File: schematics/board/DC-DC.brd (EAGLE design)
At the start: 91 x 60 mm, 130 parts

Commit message: Плата DC-DC
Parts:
- added 3,3µH: 3,3µ, CanCubeSat:B82472G6
- added 3,3µH1: 3,3µH, CanCubeSat:B82472G6
- added C40, C41, C49, C50, C56: 0,1µ, rcl:C0603
- added C44, C52: 680p, rcl:C0603
- added C45, C53: 4.7µ, rcl:C1206
- added C46: 3,3n, rcl:C0603
- added C47, C54: 150µ, CanCubeSat:ECAP150
- added C48, C55: 220µ, CanCubeSat:ECAP220
- added C57: 10µ, rcl:C1206
- added INVERT: INVERTER, CanCubeSat:SOT23-5
- added LED_G1, LED_G2, LED_R1, LED_R2: (no value), led:CHIPLED_0603
- added OPA: OPA333, CanCubeSat:SOT23-5
- added R100, R32, R33, R57: 2k, resistor:R0603
- added R28, R30, R37, R39, R67, R68, R69: 150k, resistor:R0603
- added R34, R35: 51k, resistor:R0603
- added R36, R38, R66: 10k, resistor:R0603
- added R40: 910k, resistor:R0603
- added R41: 330k, resistor:R0603
- added R65: 1M, resistor:R0603
- added R70: 24k3, resistor:R0603
- added R72: 232k, resistor:R0603
- added U$23, U$59: LTC31191, CanCubeSat:LTC3119+VIA
- added U$25: 32961, CanCubeSat:3296W
- U$2: device CanCubeSat:B82477G4 -> CanCubeSat:L_12X12
- U$3: device CanCubeSat:MP2225 -> CanCubeSat:TSOT23-8
- U$4: device CanCubeSat:SPM5020 -> CanCubeSat:L_SPM5020
- U$6, U$7: device CanCubeSat:SPM4020 -> CanCubeSat:L_SPM4020
- moved U$6 0.46 mm to (66.3, 23.6)
- moved U$4 0.28 mm to (22.2, 25.8)
- moved U$2 0.21 mm to (38.2, 23.9)
- moved U$3 0.07 mm to (8.00, 26.1)
- moved U$7 0.07 mm to (74.2, 23.6)
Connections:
- new net 1.65: R34.2, R35.1, R36.2
- new net 3.3: INVERT.P$5, OPA.P$5, R35.2
- new net 90: R65.1, R66.2, R67.2, U$59.15
- new net A: INVERT.P$2, OPA.P$1, R32.1, R37.2, R39.2, U$59.18
- new net INA_BMS+: C47.P$1, C55.P$1, R72.2, U$23.19, U$23.22, U$23.23, U$59.6, U$59.7
- new net INA_BUS+: C48.P$1, C54.P$1, R40.1, R65.2, U$23.6, U$23.7, U$25.P$3, U$59.19, U$59.22, U$59.23
- new net N$129: C41.2, U$59.3
- new net N$131: 3,3µH.2, C40.1, U$59.21, U$59.24
- new net N$132: 3,3µH.1, C41.1, U$59.5, U$59.8
- new net N$135: R69.1, U$59.13
- new net N$136: C44.1, R69.2
- new net N$139: C46.1, R66.1
- new net N$142: R68.2, U$59.17
- new net N$144: C40.2, U$59.26
- new net N$215: C53.1, C56.1, C57.1, LED_G2.A, U$23.11, U$23.15, U$23.16
- new net N$234: C45.1, LED_G1.A, U$59.11, U$59.16
- new net N$302: OPA.P$4, R36.1, R37.1
- new net N$77: 3,3µH1.2, C49.1, U$23.21, U$23.24
- new net N$78: 3,3µH1.1, C50.1, U$23.5, U$23.8
- new net N$79: R28.2, U$23.17
- new net N$80: C49.2, U$23.26
- new net N$81: R30.1, U$23.13
- new net N$82: C52.1, R30.2
- new net N$84: C50.2, U$23.3
- new net N$85: LED_R1.A, R32.2
- new net N$86: U$23.12, U$25.P$2
- new net N$87: LED_R2.A, R57.2
- new net N$89: R70.1, R72.1, U$59.12
- new net N$90: OPA.P$3, R38.1, R39.1
- new net N$91: LED_G1.C, R100.2
- new net N$92: LED_G2.C, R33.2
- new net PGOOD1: LED_R1.C, U$59.10
- new net PGOOD2: LED_R2.C, U$23.10
- new net RUN: R38.2, R40.2, R41.1
- new net Y: INVERT.P$4, R57.1, U$23.18
- net GND: now also C44.2, C45.2, C46.2, C47.P$2, C48.P$2, C52.2, C53.2, C54.P$2, C55.P$2, C56.2, C57.2, INVERT.P$3, OPA.P$2, R100.1, R28.1, R33.1, R34.1, R41.2, R67.1, R68.1, R70.2, U$23.14, U$23.20, U$23.25, U$23.28, U$23.29, U$23.4, U$23.9, U$23.P$1, U$23.P$10, U$23.P$2, U$23.P$3, U$23.P$4, U$23.P$5, U$23.P$6, U$23.P$7, U$23.P$8, U$23.P$9, U$25.P$1, U$59.14, U$59.20, U$59.25, U$59.28, U$59.29, U$59.4, U$59.9, U$59.P$1, U$59.P$10, U$59.P$2, U$59.P$3, U$59.P$4, U$59.P$5, U$59.P$6, U$59.P$7, U$59.P$8, U$59.P$9
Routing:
- net GND: track 57.0 -> 167.3 mm, vias 54 -> 63
- net INA_BUS+: track 0.00 -> 95.3 mm, vias 0 -> 9
- net INA_BMS+: track 0.00 -> 78.7 mm, vias 0 -> 7
- net A: track 0.00 -> 65.3 mm, vias 0 -> 4
- net Y: track 0.00 -> 48.8 mm, vias 0 -> 4
- net PGOOD2: track 0.00 -> 35.8 mm, vias 0 -> 2
- net PGOOD1: track 0.00 -> 32.1 mm, vias 0 -> 2
- net 3.3: track 0.00 -> 20.9 mm, vias 0 -> 1
- net N$234: track 0.00 -> 19.3 mm, vias 0 -> 2
- net 90: track 0.00 -> 18.2 mm, vias 0 -> 3
- net N$215: track 0.00 -> 18.1 mm, vias 0 -> 2
- net N$86: track 0.00 -> 14.3 mm
- net N$89: track 0.00 -> 11.7 mm
- net N$142: track 0.00 -> 9.93 mm
- net N$79: track 0.00 -> 9.65 mm
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- added copper zone on layer 1, net INA_BMS+
- added copper zone on layer 16, net INA_BMS+
- added copper zone on layer 1, net INA_BUS+
- added copper zone on layer 16, net INA_BUS+
- added copper zone on layer 1, net N$131
- added copper zone on layer 1, net N$132
- added copper zone on layer 1, net N$215
- added copper zone on layer 1, net N$234
- added copper zone on layer 1, net N$77
- added copper zone on layer 1, net N$78
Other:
- board size 91 x 60 mm -> 91 x 91 mm
- board text added: "BMS+"
- board text added: "BUS+"

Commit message: платы DC-DC и AB
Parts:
- removed D1: MBR0520LT, diode:SOD123
- added D2: (no value), diode:SMC
- moved C2 7.20 mm to (35.9, 44.6)
- moved C36 7.20 mm to (45.6, 45.2)
- moved C4 7.20 mm to (41.0, 51.2)
- moved R10 7.20 mm to (48.0, 45.2)
- moved R3 7.20 mm to (43.3, 51.0)
- moved R4 7.20 mm to (46.0, 41.2)
- moved R6 7.20 mm to (35.9, 48.6)
- moved R7 7.20 mm to (33.5, 48.6)
- moved U$1 7.20 mm to (41.0, 44.2)
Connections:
- net GND: now also D2.A; no longer D1.A
- net N$6: now also D2.C; no longer D1.C
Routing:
- net N$8: track 5.22 -> 12.4 mm
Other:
- outline, holes or cut-outs redrawn
- board text added: "LTC3119"
- board text added: "LTC3633"
- board text added: "LTC3633 on board"
- board text added: "MP1584"
- board text added: "MP2225"

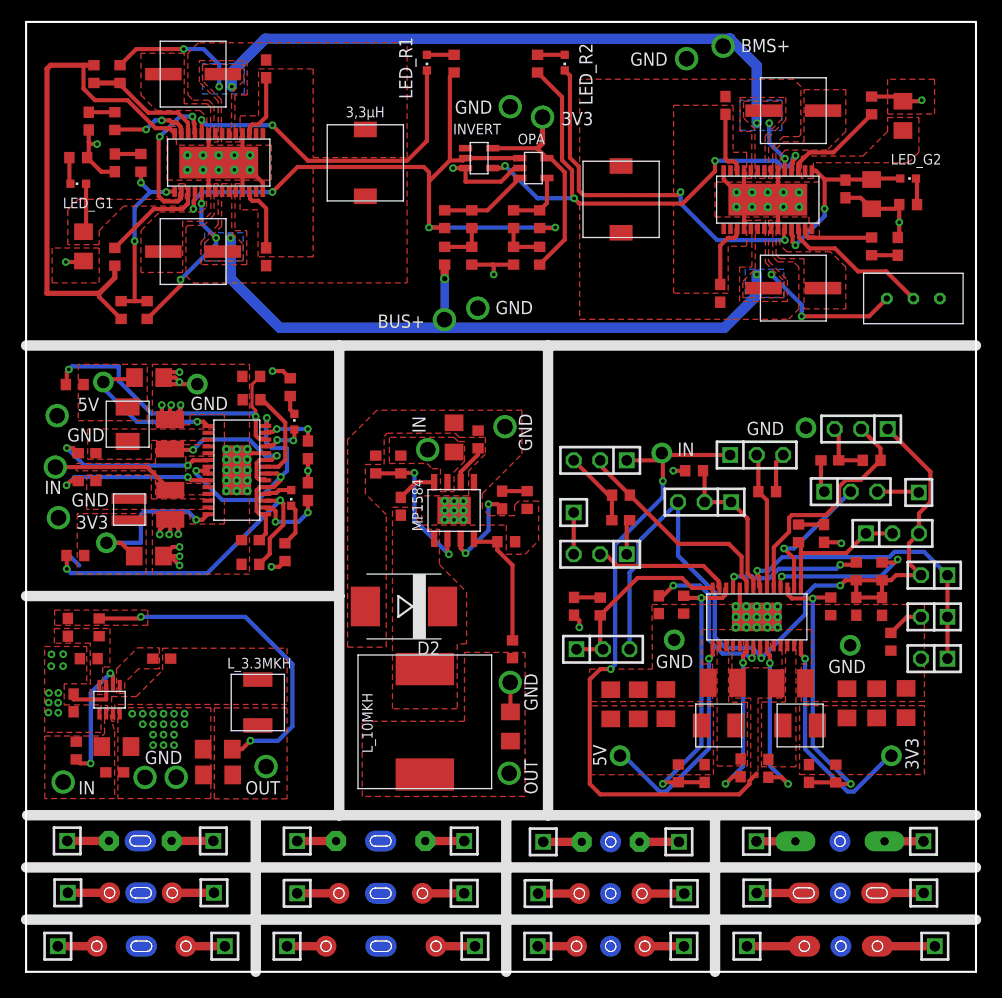
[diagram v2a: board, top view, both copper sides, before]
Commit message: Добавлены предохранители в библиотеку
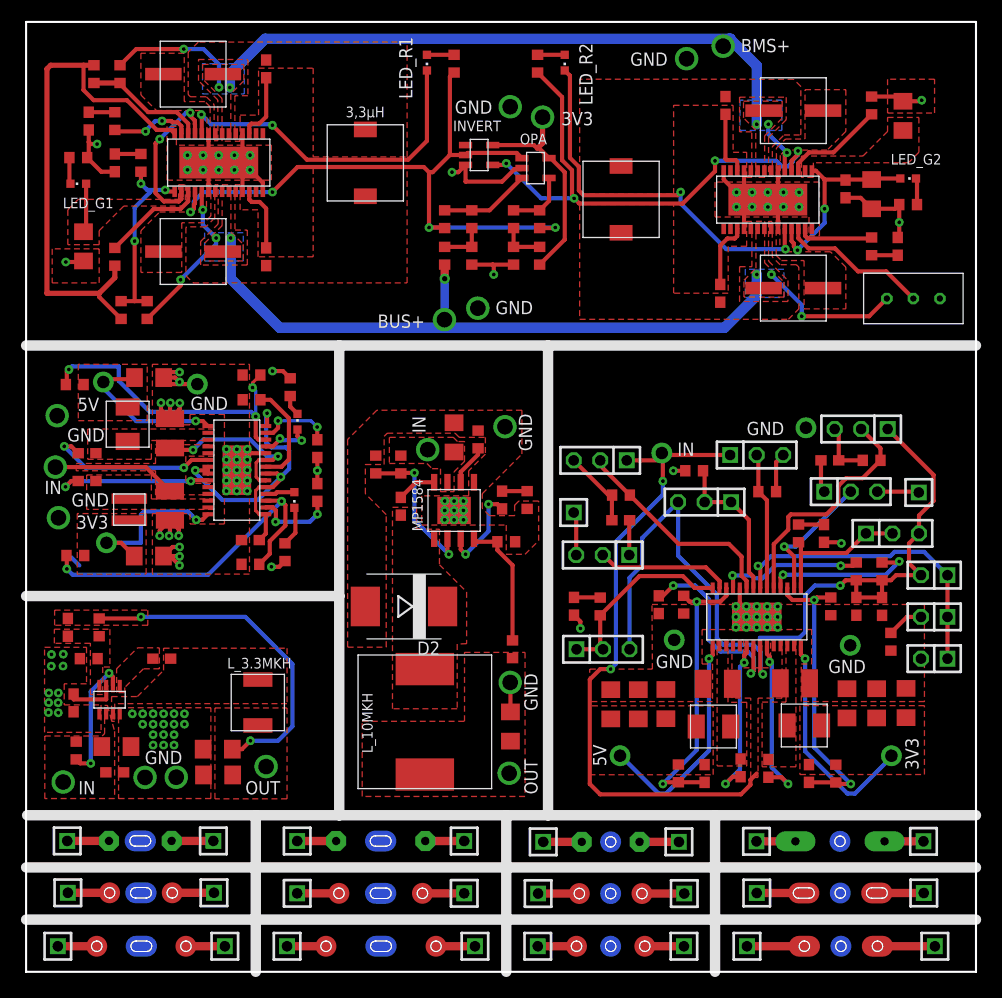
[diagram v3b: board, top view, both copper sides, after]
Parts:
- moved C37 0.91 mm to (27.9, 50.1)
- moved C35 0.90 mm to (27.9, 45.9)
- moved C39 0.51 mm to (66.2, 27.6)
- moved U$6 0.51 mm to (65.8, 23.5)
- moved C38 0.40 mm to (73.7, 27.6)
- moved U$7 0.40 mm to (74.5, 23.6)
- moved LED1 0.36 mm to (25.7, 45.2)
- moved LED2 0.30 mm to (26.0, 52.7)
- moved INVERT 0.30 mm to (43.4, 78.2)
- moved JP8 0.25 mm to (55.2, 39.9)
- moved OPA 0.20 mm to (48.8, 77.0)
- moved R9 0.13 mm to (21.6, 57.2)
- moved C17 0.10 mm to (13.8, 51.6)
- moved C16 0.09 mm to (13.8, 44.6)
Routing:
- net INTVCC: track 79.5 -> 84.7 mm
- net N$27: track 16.0 -> 19.0 mm
- net N$52: track 5.34 -> 7.28 mm
- net GND: track 167.3 -> 169.1 mm
- net N$24: track 31.0 -> 32.3 mm
- net PGOOD2: track 35.8 -> 37.1 mm
- net Y: track 48.8 -> 50.0 mm
- net N$51: track 6.73 -> 7.76 mm
- net N$3: track 4.07 -> 5.09 mm
- net N$215: track 18.1 -> 19.0 mm
- net N$1: track 9.00 -> 9.91 mm
- net N$32: track 15.7 -> 16.5 mm
- net PGOOD1: track 32.1 -> 32.7 mm
- net N$234: track 19.3 -> 19.8 mm
- net N$39: track 29.6 -> 29.8 mm, vias 2 -> 3
